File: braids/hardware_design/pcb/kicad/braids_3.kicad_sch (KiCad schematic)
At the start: 55 parts

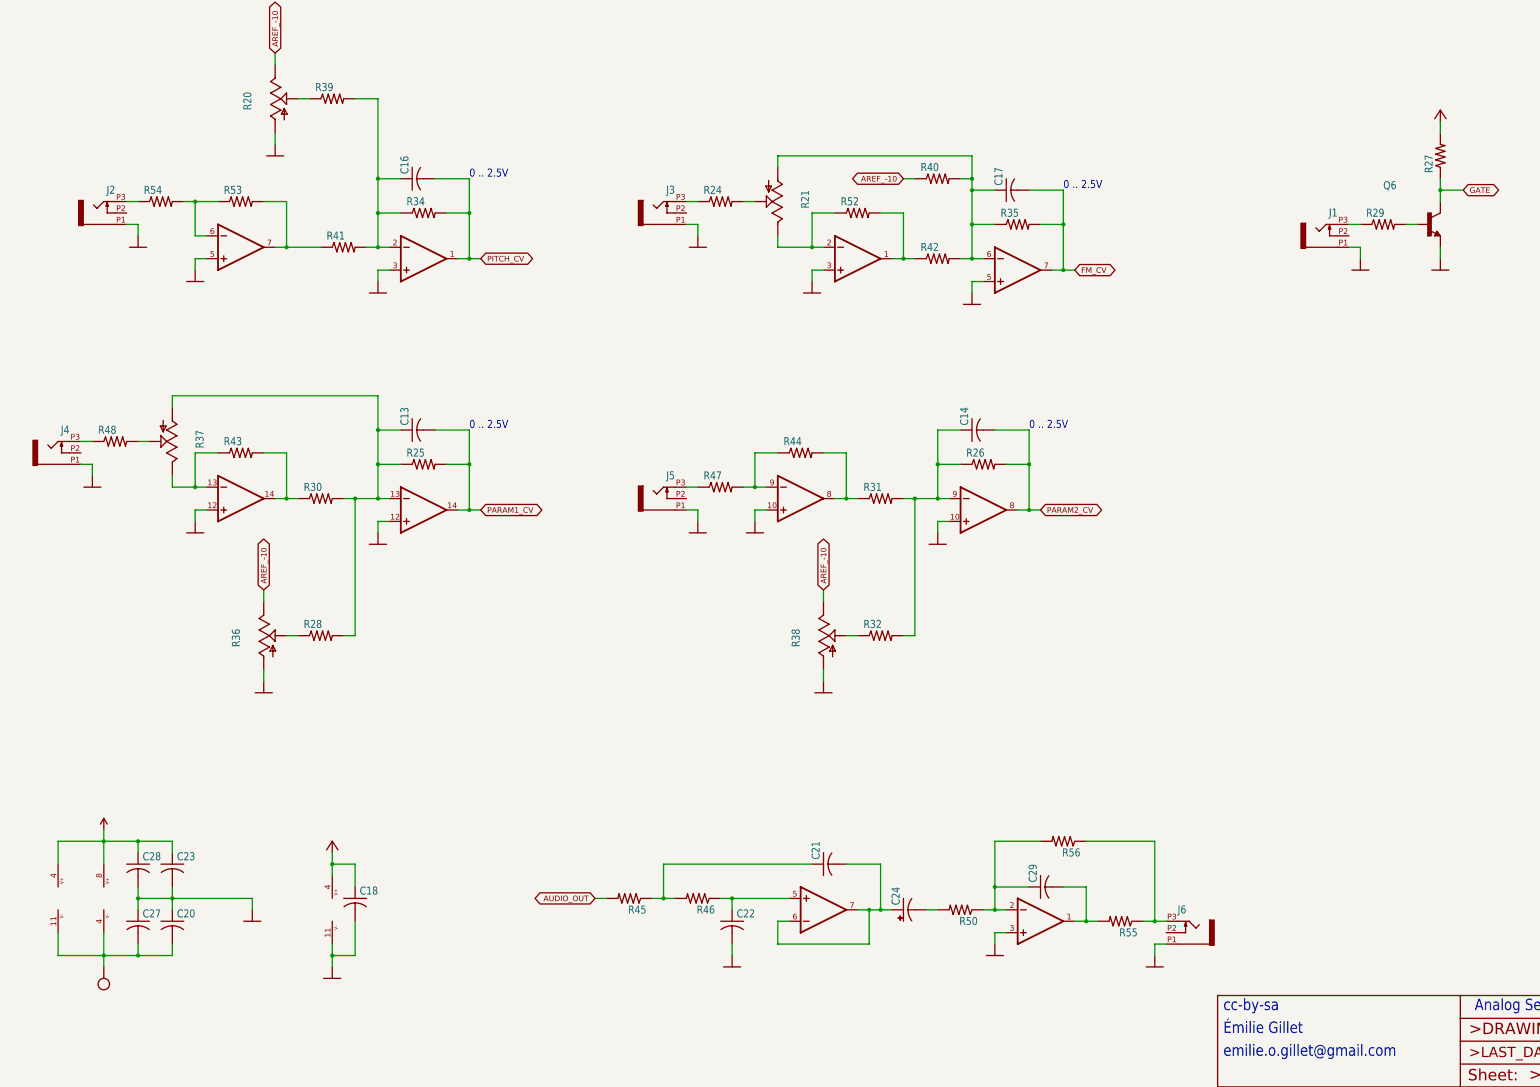
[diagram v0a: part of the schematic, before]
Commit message: changed mcp3204 to mcp3208
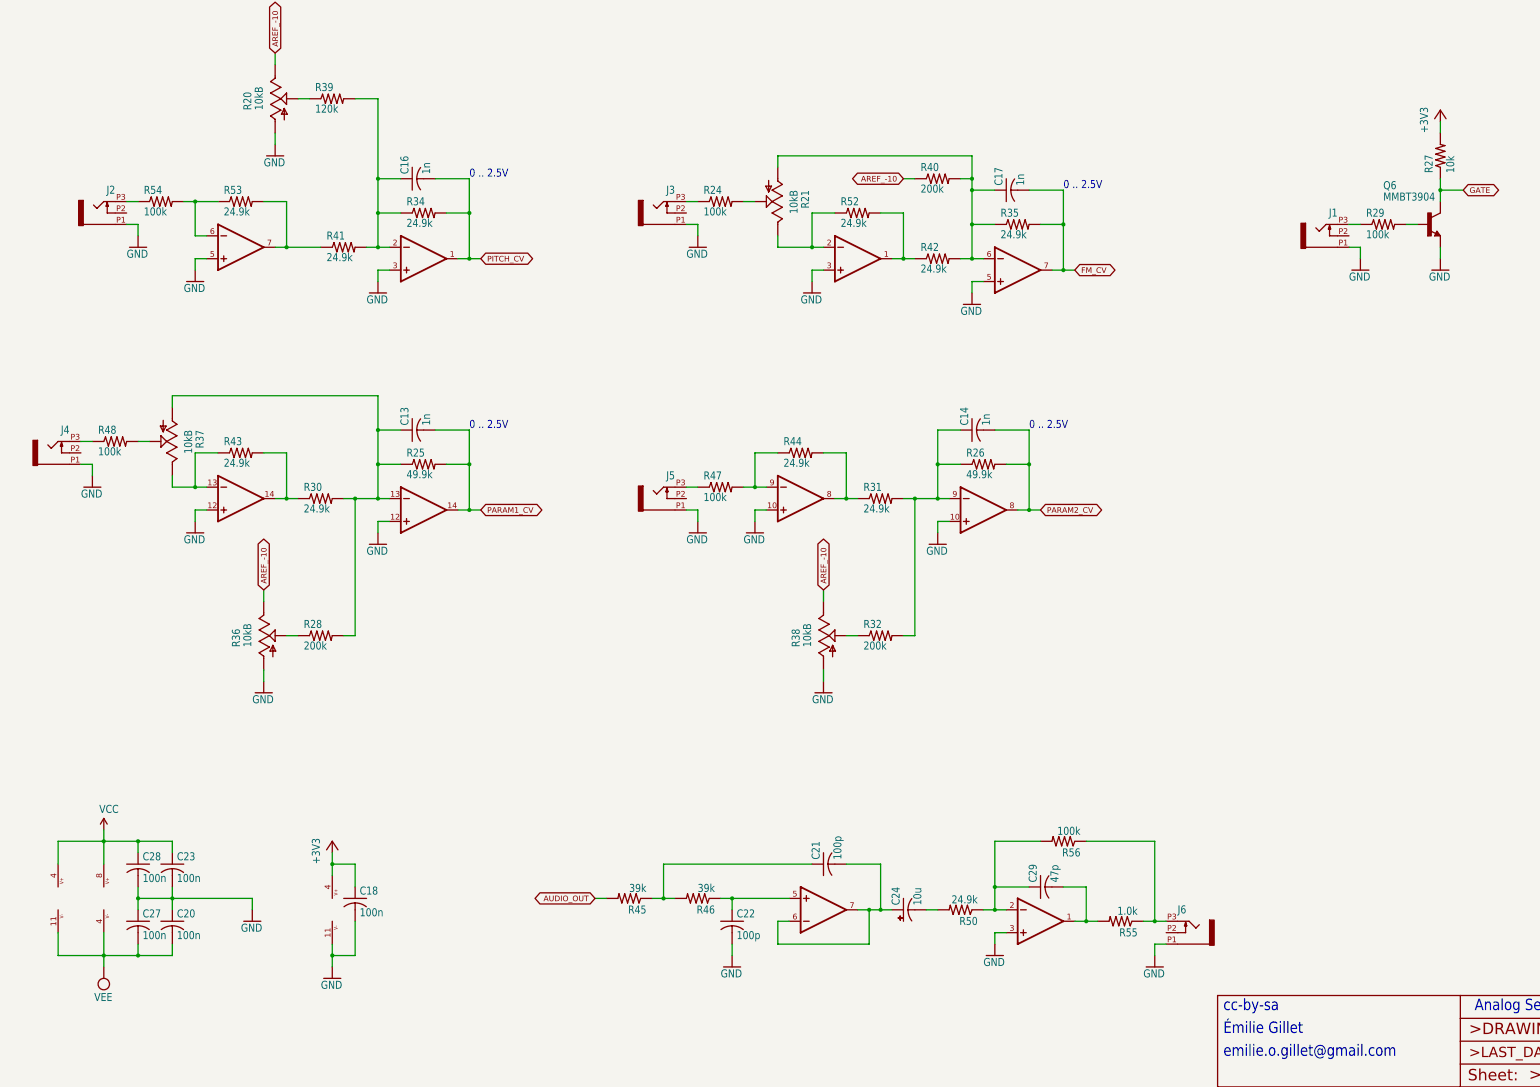
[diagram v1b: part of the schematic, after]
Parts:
- C13, C14, C16, C17: value (none) -> 1n; footprint (none) -> braids:C0603
- C18, C20, C23, C27, C28: value (none) -> 100n; footprint (none) -> braids:C0603
- C21, C22: value (none) -> 100p; footprint (none) -> braids:C0603
- C24: value (none) -> 10u; footprint (none) -> braids:PANASONIC_B
- C29: value (none) -> 47p; footprint (none) -> braids:C0603
- IC10: value (none) -> TL072; footprint (none) -> braids:SO08
- IC7: value (none) -> MCP6004; footprint (none) -> braids:SO14
- IC9: value (none) -> TL074D; footprint (none) -> braids:SO14
- J1, J2, J3, J4, J5, J6: value (none) -> PJ301_THONKICONN6; footprint (none) -> braids:WQP_PJ_301M6
- Q6: value (none) -> MMBT3904; footprint (none) -> braids:SOT23-BEC
- R20, R21, R36, R37, R38: value (none) -> 10kB; footprint (none) -> braids:ALPS_POT_VERTICAL_PS
- R24, R29, R47, R48, R54, R56: value (none) -> 100k; footprint (none) -> braids:R0603
- R25, R26: value (none) -> 49.9k; footprint (none) -> braids:R0603
- R27: value (none) -> 10k; footprint (none) -> braids:R0603
- R28, R32, R40: value (none) -> 200k; footprint (none) -> braids:R0603
- R30, R31, R34, R35, R41, R42, R43, R44, R50, R52, R53: value (none) -> 24.9k; footprint (none) -> braids:R0603
- R39: value (none) -> 120k; footprint (none) -> braids:R0603
- R45, R46: value (none) -> 39k; footprint (none) -> braids:R0603
- R55: value (none) -> 1.0k; footprint (none) -> braids:R0603
